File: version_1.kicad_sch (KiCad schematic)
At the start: 27 parts, among them U1 Pico, U10 74AHC595, U12 C967633

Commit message: added moany componaets
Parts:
- removed R27: 1k, Resistor_SMD:R_0603_1608Metric_Pad0.98x0.95mm_HandSolder, symbol Device:R
- added U18: SM04B-SRSS-TB_(LF)(SN), footprint:CONN-SMD_4P-P1.00_SM04B-SRSS-TB-LF-SN, symbol SM04B-SRSS-TB_(LF)(SN):SM04B-SRSS-TB_(LF)(SN)
- R25: value 1k -> 10k
- R26: value 1k -> 33k
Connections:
- net Untitled Sheet5/PWM is gone; now on net Servo/PWM: U10.3 (QD)
- net Untitled Sheet5/PWR is gone; now on net Servo/PWR: U10.2 (QC)
- net +3.3V: now also U18.2
- net ENCODER7: now also U1.11 (GPIO8); no longer U1.29 (GPIO22)
- net GND: now also U18.1
- net SCL: now also U18.4
- net SDA: now also U18.3
- net Servo/PWM: no longer U10.1 (QB)
- net Servo/PWR: no longer U10.15 (QA)
- net VCC: now also R26.1
- net Power/Pgood: now also U1.29 (GPIO22); no longer U1.11 (GPIO8)
- new net Servo/PWM: U10.1 (QB)
- new net Servo/PWR: U10.15 (QA)
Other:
- sheet Untitled Sheet renamed Motor Driver
- sheet Untitled Sheet1 renamed Motor Driver2
- sheet Untitled Sheet6 renamed Servo
- sheet power renamed Power
- removed sheet Untitled Sheet5
- removed sheet motor_decoupling
- removed sheet motor_decoupling1
- removed sheet motor_decoupling2
- note added: "TODO: Change hbduege"
- note added: "TODO: Change power converter"
- note added: "TODO: Check volatges on bus"
- moved on the sheet: D5, D6, H1, H2, H3, H4, R21, R22, R23, R25, R26, U1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

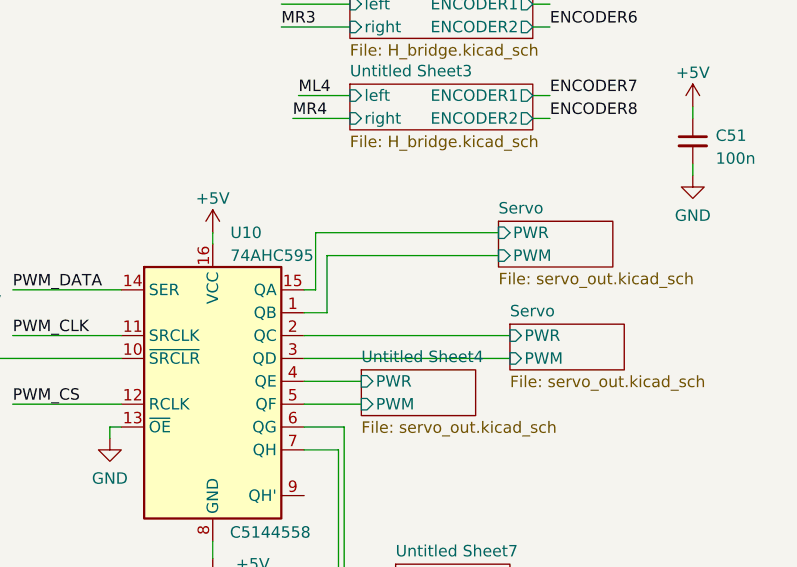
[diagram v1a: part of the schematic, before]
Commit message: specified correct shift register
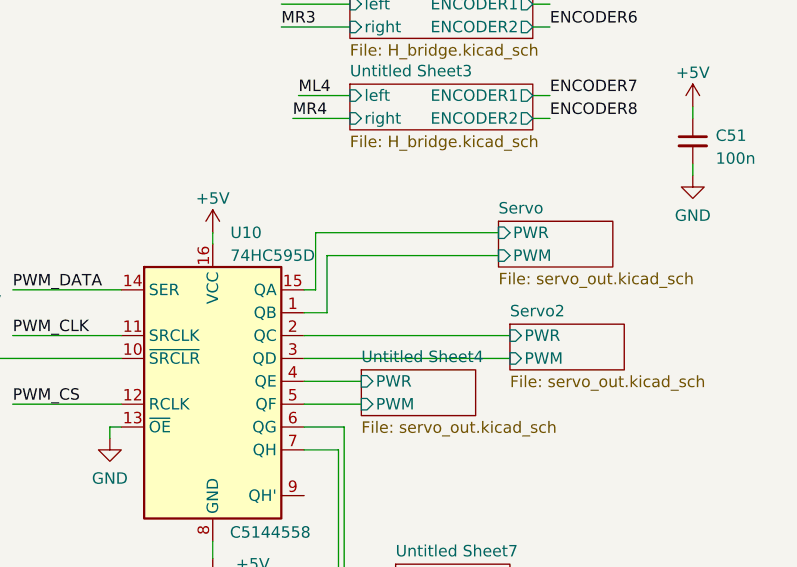
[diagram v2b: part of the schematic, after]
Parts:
- U10: value 74AHC595 -> 74HC595D; JLCPCB Part# C2682116 -> C5144558
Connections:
- net Servo/PWM renamed Servo2/PWM
- net Servo/PWR renamed Servo2/PWR
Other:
- added sheet Servo2 (servo_out.kicad_sch)
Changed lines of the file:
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@@
       (effects (font (size 1.27 1.27)) (justify left))
     )
-    (property "Value" "74AHC595" (at 228.0159 80.01 0)
+    (property "Value" "74HC595D" (at 228.0159 80.01 0)
       (effects (font (size 1.27 1.27)) (justify left))
     )
@@
       (effects (font (size 1.27 1.27)) hide)
     )
-    (property "Datasheet" "https://assets.nexperia.com/documents/data-sheet/74AHC_AHCT595.pdf" (at 226.06 93.98 0)
-      (effects (font (size 1.27 1.27)) hide)
-    )
-    (property "JLCPCB Part#" "C2682116" (at 226.06 93.98 0)
+    (property "Datasheet" "https://wmsc.lcsc.com/wmsc/upload/file/pdf/v2/lcsc/2401041538_JSMSEMI-74HC595D_C5144558.pdf" (at 226.06 93.98 0)
+      (effects (font (size 1.27 1.27)) hide)
+    )
+    (property "JLCPCB Part#" "C5144558" (at 226.06 93.98 0)
       (effects (font (size 1.27 1.27)) hide)
     )
@@
     (stroke (width 0.1524) (type solid))
     (fill (color 0 0 0 0.0000))
-    (property "Sheetname" "Servo" (at 259.08 86.9184 0)
+    (property "Sheetname" "Servo2" (at 259.08 86.9184 0)
       (effects (font (size 1.27 1.27)) (justify left bottom))
     )

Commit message: added more symbols
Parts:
- added C5: 100n, Capacitor_SMD:C_0603_1608Metric_Pad1.08x0.95mm_HandSolder, symbol Device:C_Small
- added C6: 330n, Capacitor_SMD:C_0603_1608Metric_Pad1.08x0.95mm_HandSolder, symbol Device:C_Small
- added JP1, JP2, JP3: Jumper_3_Bridged12, Jumper:SolderJumper-3_P1.3mm_Bridged12_RoundedPad1.0x1.5mm, symbol Jumper:Jumper_3_Bridged12
- added U3: L7805CD2T-TR, footprint:TO-263-2_L10.0-W9.1-P5.08-LS15.2-TL, symbol my_symbols:L7805CD2T-TR
- U10: value 74HC595D -> 74HCT595D; JLCPCB Part# C5144558 -> C282339
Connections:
- net +3.3V: now also JP2.3 (B), JP3.1 (A)
- net +5V: no longer D5.2 (A)
- net GND: now also C5.2, C6.2, JP2.1 (A), JP3.3 (B), U3.4 (GND)
- net VCC: now also C6.1, U3.1 (IN)
- new net: C5.1, JP1.1 (A), U3.3 (OUT)
- new net: D5.2 (A), JP1.2 (C)
- new net 1S: JP1.3 (B)
- new net ENC_PWR_1: JP3.2 (C)
- new net ENC_PWR_2: JP2.2 (C)
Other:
- note added: "Also works C5144558"
- note removed: "C5144558"
- note removed: "TODO: Change hbduege"
- note removed: "TODO: Check volatges on bus"
- moved on the sheet: C29, C51, U10

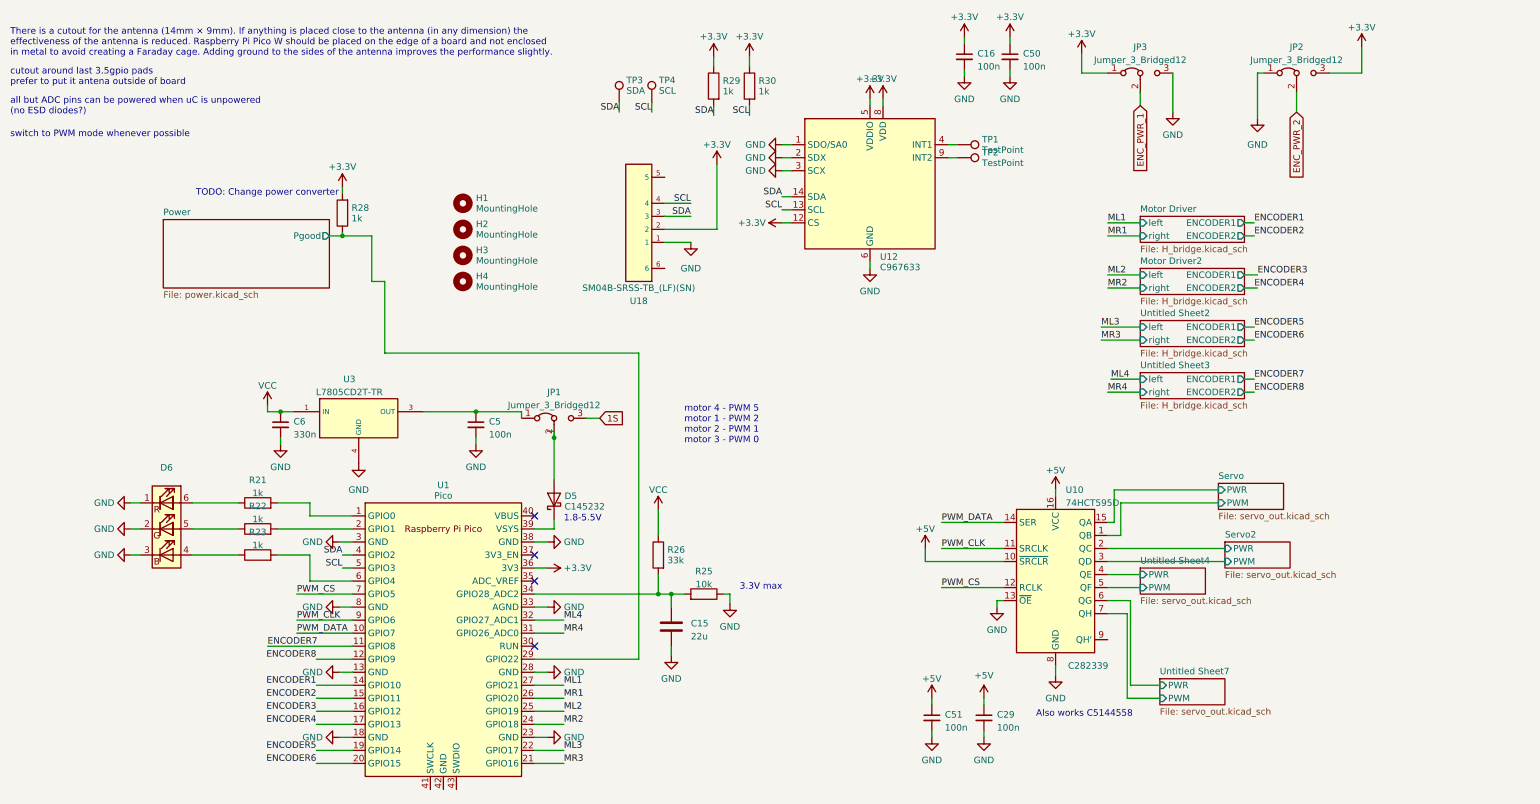
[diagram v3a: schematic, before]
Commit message: Added thing for servo pwoer
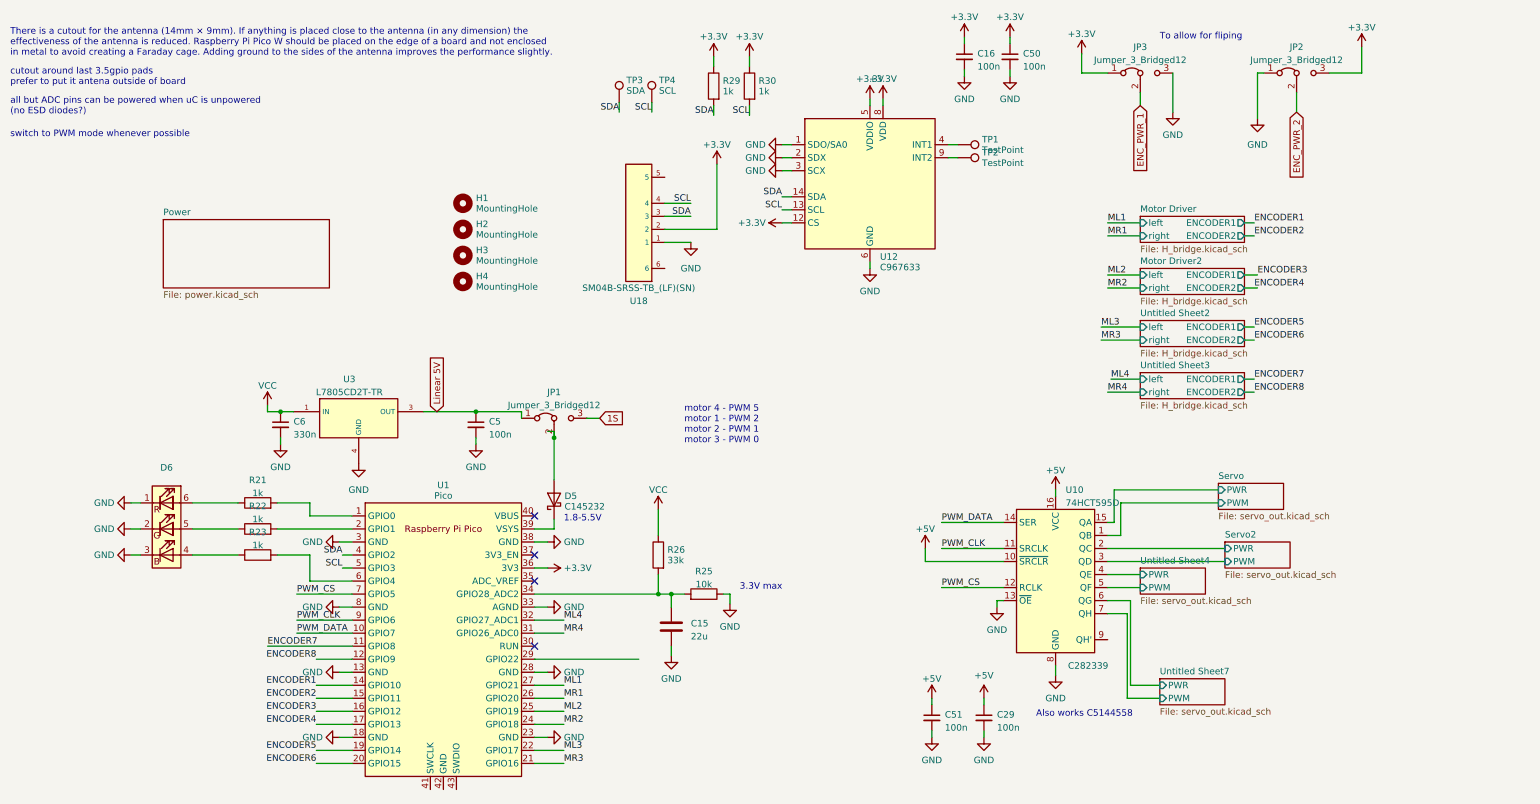
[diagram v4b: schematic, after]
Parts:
- removed R28: 1k, Resistor_SMD:R_0603_1608Metric_Pad0.98x0.95mm_HandSolder, symbol Device:R
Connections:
- net Linear 5V: now reaches C5.1, JP1.1 (A), U3.3 (OUT)
- net Power/Pgood: no longer names the net of U1.29 (GPIO22)
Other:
- sheet Power ports: added none; removed Pgood
- note added: "To allow for fliping"
- note removed: "TODO: Change power converter"
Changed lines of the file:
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@@
   (junction (at 144.78 127) (diameter 0) (color 0 0 0 0)
   )
-  (junction (at 83.185 57.15) (diameter 0) (color 0 0 0 0)
-  )
   (junction (at 71.12 91.44) (diameter 0) (color 0 0 0 0)
   )
@@
     (stroke (width 0) (type default))
   )
-  (wire (pts (xy 140.97 80.01) (xy 140.97 139.7))
-    (stroke (width 0) (type default))
-  )
   (wire (pts (xy 262.89 25.4) (xy 261.62 25.4))
     (stroke (width 0) (type default))
@@
     (stroke (width 0) (type default))
   )
-  (wire (pts (xy 83.185 47.625) (xy 83.185 48.895))
-    (stroke (width 0) (type default))
-  )
   (wire (pts (xy 275.59 25.4) (xy 281.94 25.4))
     (stroke (width 0) (type default))
@@
     (stroke (width 0) (type default))
   )
-  (wire (pts (xy 140.97 80.01) (xy 91.44 80.01))
-    (stroke (width 0) (type default))
-  )
   (wire (pts (xy 83.185 121.92) (xy 85.09 121.92))
     (stroke (width 0) (type default))
@@
     (stroke (width 0) (type default))
   )
-  (wire (pts (xy 88.9 57.15) (xy 83.185 57.15))
-    (stroke (width 0) (type default))
-  )
   (wire (pts (xy 123.19 95.25) (xy 124.46 95.25))
     (stroke (width 0) (type default))
@@
     (stroke (width 0) (type default))
   )
-  (wire (pts (xy 91.44 66.04) (xy 91.44 80.01))
-    (stroke (width 0) (type default))
-  )
   (wire (pts (xy 222.25 106.68) (xy 222.25 107.95))
     (stroke (width 0) (type default))
@@
     (stroke (width 0) (type default))
   )
-  (wire (pts (xy 80.645 57.15) (xy 83.185 57.15))
-    (stroke (width 0) (type default))
-  )
   (wire (pts (xy 168.91 41.91) (xy 170.815 41.91))
     (stroke (width 0) (type default))
@@
     (stroke (width 0) (type default))
   )
-  (wire (pts (xy 88.9 66.04) (xy 88.9 57.15))
-    (stroke (width 0) (type default))
-  )
   (wire (pts (xy 162.56 31.75) (xy 162.56 33.655))
     (stroke (width 0) (type default))
   )
-  (wire (pts (xy 88.9 66.04) (xy 91.44 66.04))
-    (stroke (width 0) (type default))
-  )
   (wire (pts (xy 78.105 160.02) (xy 85.09 160.02))
     (stroke (width 0) (type default))
@@
     (stroke (width 0) (type default))
   )
-  (wire (pts (xy 83.185 57.15) (xy 83.185 56.515))
-    (stroke (width 0) (type default))
-  )
   (wire (pts (xy 155.575 22.225) (xy 155.575 24.13))
     (stroke (width 0) (type default))
@@
     (effects (font (size 1.27 1.27)) (justify left bottom))
   )
+  (text "To allow for fliping" (at 242.57 19.05 0)
+    (effects (font (size 1.27 1.27)) (justify left bottom))
+  )
   (text "3.3V max" (at 160.655 126.365 0)
     (effects (font (size 1.27 1.27)) (justify left bottom))
@@
     (effects (font (size 1.27 1.27)) (justify left bottom))
   )
-  (text "TODO: Change power converter" (at 54.61 49.53 0)
-    (effects (font (size 1.27 1.27)) (justify left bottom))
-  )
   (text "Also works C5144558" (at 218.44 151.13 0)
     (effects (font (size 1.27 1.27)) (justify left bottom))
@@
     )
   )
+  (global_label "Linear 5V" (shape input) (at 101.6 91.44 90) (fields_autoplaced)
+    (effects (font (size 1.27 1.27)) (justify left))
+    (property "Intersheetrefs" "${INTERSHEET_REFS}" (at 101.6 79.4628 90)
+      (effects (font (size 1.27 1.27)) (justify left) hide)
+    )
+  )
   (global_label "1S" (shape input) (at 133.35 92.71 0) (fields_autoplaced)
     (effects (font (size 1.27 1.27)) (justify left))
@@
     )
   )
-  (symbol (lib_id "power:+3.3V") (at 83.185 47.625 0) (unit 1)
-    (in_bom yes) (on_board yes) (dnp no) (fields_autoplaced)
-    (property "Reference" "#PWR070" (at 83.185 51.435 0)
-      (effects (font (size 1.27 1.27)) hide)
-    )
-    (property "Value" "+3.3V" (at 83.185 43.68 0)
-      (effects (font (size 1.27 1.27)))
-    )
-    (property "Footprint" "" (at 83.185 47.625 0)
-      (effects (font (size 1.27 1.27)) hide)
-    )
-    (property "Datasheet" "" (at 83.185 47.625 0)
-      (effects (font (size 1.27 1.27)) hide)
-    )
-    (pin "1")
-    (instances
-      (project "version_1"
-        (path "/23ba0750-4a55-4d50-828b-749cc0fbb8c8/9789521c-7f58-473a-9dd2-6c6a71290f6c"
-          (reference "#PWR070") (unit 1)
-        )
-        (path "/23ba0750-4a55-4d50-828b-749cc0fbb8c8"
-          (reference "#PWR0158") (unit 1)
-        )
-      )
-    )
-  )
   (symbol (lib_id "Mechanical:MountingHole") (at 106.68 55.88 0) (unit 1)
     (in_bom yes) (on_board yes) (dnp no) (fields_autoplaced)
@@
     )
   )
-  (symbol (lib_id "Device:R") (at 83.185 52.705 180) (unit 1)
-    (in_bom yes) (on_board yes) (dnp no) (fields_autoplaced)
-    (property "Reference" "R28" (at 84.963 51.681 0)
-      (effects (font (size 1.27 1.27)) (justify right))
-    )
-    (property "Value" "1k" (at 84.963 53.729 0)
-      (effects (font (size 1.27 1.27)) (justify right))
-    )
-    (property "Footprint" "Resistor_SMD:R_0603_1608Metric_Pad0.98x0.95mm_HandSolder" (at 84.963 52.705 90)
-      (effects (font (size 1.27 1.27)) hide)
-    )
-    (property "Datasheet" "~" (at 83.185 52.705 0)
-      (effects (font (size 1.27 1.27)) hide)
-    )
-    (pin "1")
-    (pin "2")
-    (instances
-      (project "version_1"
-        (path "/23ba0750-4a55-4d50-828b-749cc0fbb8c8"
-          (reference "R28") (unit 1)
-        )
-        (path "/23ba0750-4a55-4d50-828b-749cc0fbb8c8/9789521c-7f58-473a-9dd2-6c6a71290f6c"
-          (reference "R18") (unit 1)
-        )
-      )
-    )
-  )
   (symbol (lib_id "Connector:TestPoint") (at 203.2 39.37 270) (unit 1)
     (in_bom yes) (on_board yes) (dnp no) (fields_autoplaced)
@@
       (effects (font (size 1.27 1.27)) hide)
     )
-    (pin "Pgood" output (at 80.645 57.15 0)
-      (effects (font (size 1.27 1.27)) (justify right))
-    )
     (instances
